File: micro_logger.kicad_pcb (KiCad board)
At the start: 2 copper layers, 16.8 x 27.4 mm, 25 parts, among them J3 ISP, J4 Conn_01x02, J5 DM3AT-SF-PEJM5, SW2 SW_Push, U1 MIC5205-3.3, U2 MPU-9250, U3 ATMEGA328-AU, Y1 Crystal_GND2

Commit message: updated shift logic
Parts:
- removed G***: LOGO, Symbol:gait_logo
- added C11: .1uF, Capacitor_SMD:C_0603_1608Metric, F.Cu at (150.7, 101.8)
- added C12: .1uF, Capacitor_SMD:C_0603_1608Metric, F.Cu at (148.3, 101.0)
- added C13: 100pF, Capacitor_SMD:C_0603_1608Metric, F.Cu at (140.8, 91.2)
- added C7: 1uF, Capacitor_SMD:C_0603_1608Metric, F.Cu at (141.3, 100.4)
- added R5: 10K, Resistor_SMD:R_0805_2012Metric, F.Cu at (140.9, 97.0)
- added R6: 10K, Resistor_SMD:R_0805_2012Metric, F.Cu at (146.5, 94.7)
- added R7: 200K, Resistor_SMD:R_0805_2012Metric, F.Cu at (149.2, 97.3)
- added U4: ICM-20948, components:ICM-20948, F.Cu at (145.2, 100.1)
- added U5: PCA9306, Package_SO:VSSOP-8_2.3x2mm_P0.5mm, F.Cu at (144.3, 94.6)
- C2: value 10nF -> 1uF
- R1, R2: value 10k -> 10K
- R4: footprint Resistor_SMD:R_0805_2012Metric_Pad1.15x1.40mm_HandSolder -> Resistor_SMD:R_0805_2012Metric
- U2: value MPU-9250 -> TLV70218_SOT23-5; footprint Package_DFN_QFN:QFN-24-1EP_3x3mm_P0.4mm_EP1.75x1.6mm -> Package_TO_SOT_SMD:SOT-23-5
- moved R9 16.6 mm to (148.5, 80.0), turned to 270 degrees
- moved C8 14.0 mm to (140.7, 82.4), turned to 180 degrees
- moved C2 10.0 mm to (141.4, 98.9), turned to 180 degrees
- moved C5 8.14 mm to (141.3, 102.0), turned to 0 degrees
- moved C6 7.23 mm to (150.7, 100.2)
- moved R2 5.80 mm to (149.3, 95.2), turned to 180 degrees
- moved U2 5.64 mm to (140.9, 94.1), turned to 180 degrees
- moved C9 3.57 mm to (139.7, 85.6)
- moved C1 2.38 mm to (144.5, 79.4)
- moved SW2 1.75 mm to (153.7, 99.1), turned to 270 degrees
- moved R1 1.74 mm to (149.3, 93.3)
- moved C3 1.46 mm to (140.0, 77.9)
- moved U1 1.20 mm to (147.4, 75.7)
- moved R4 0.77 mm to (153.1, 94.8)
- moved J3 0.67 mm to (150.9, 76.7)
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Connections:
- C2 pad 1: GND -> +3V3
- C2 pad 2: +3V3 -> GND
- C6 pad 1: GND -> +3V3
- C6 pad 2: +3V3 -> GND
- U2 pad 2: (no net) -> GND
- U2 pad 3: (no net) -> +3V3
- U2 pad 5: (no net) -> +1V8
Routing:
- net +1V8: track 0.00 -> 38.0 mm, vias 0 -> 4
- net GND: track 42.3 -> 71.0 mm, vias 14 -> 12
- net Net-(C13-Pad1): track 0.00 -> 14.2 mm, vias 0 -> 2
- net +3V3: track 81.2 -> 89.4 mm, vias 3 -> 4
- net MISO: track 17.8 -> 24.7 mm
- net /Ardunio/RESET: track 25.0 -> 31.4 mm, vias 2 -> 1
- net SCK: track 27.8 -> 33.0 mm, vias 1 -> 2
- net Net-(R5-Pad2): track 0.00 -> 5.20 mm
- net Net-(R6-Pad2): track 0.00 -> 4.33 mm
- net SDA_MPU: track 4.20 -> 8.33 mm
- net /Ardunio/D2: track 9.24 -> 12.9 mm, vias 0 -> 2
- net MOSI: track 18.6 -> 16.2 mm, vias 1 -> 2
- net VCC: track 17.0 -> 19.3 mm, vias 1 -> 2
- net Net-(U3-Pad7): track 2.78 -> 3.57 mm
- net Net-(C9-Pad1): track 2.53 -> 3.23 mm
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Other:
- board size 16.8 x 27.4 mm -> 17.5 x 29.5 mm

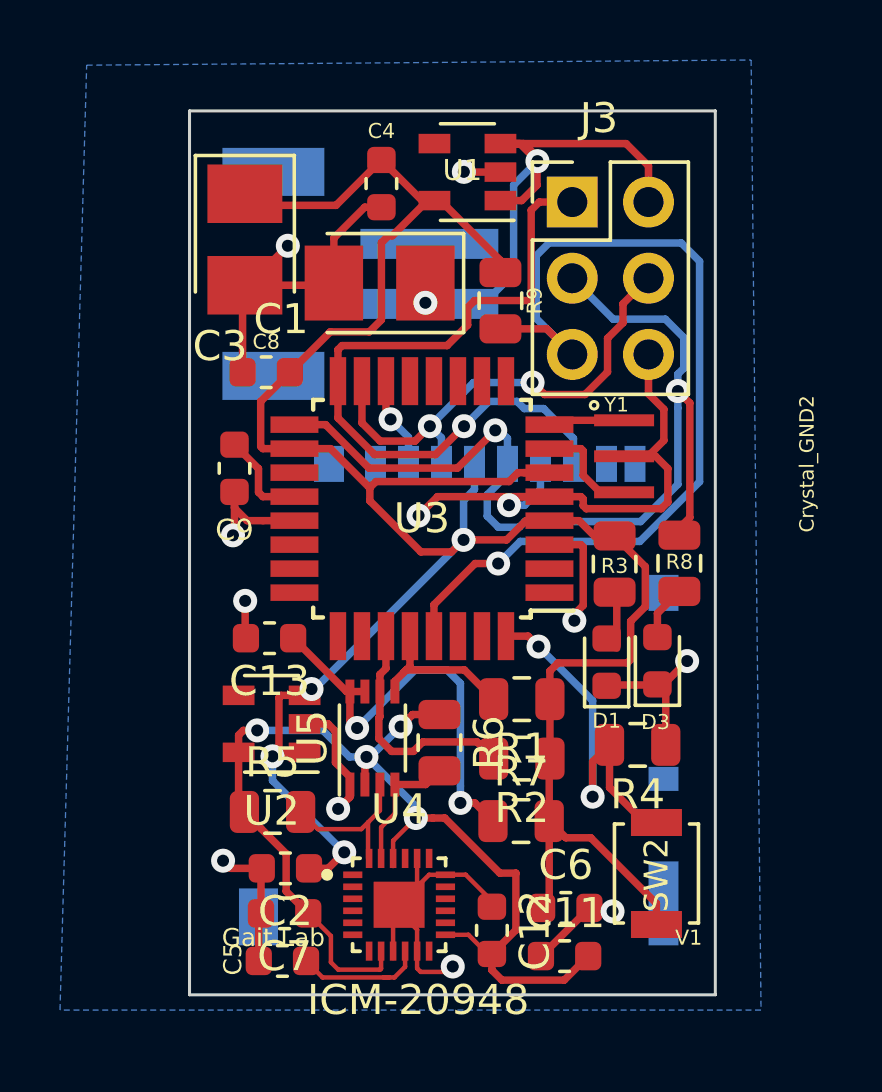
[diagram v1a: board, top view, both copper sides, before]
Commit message: updated layout
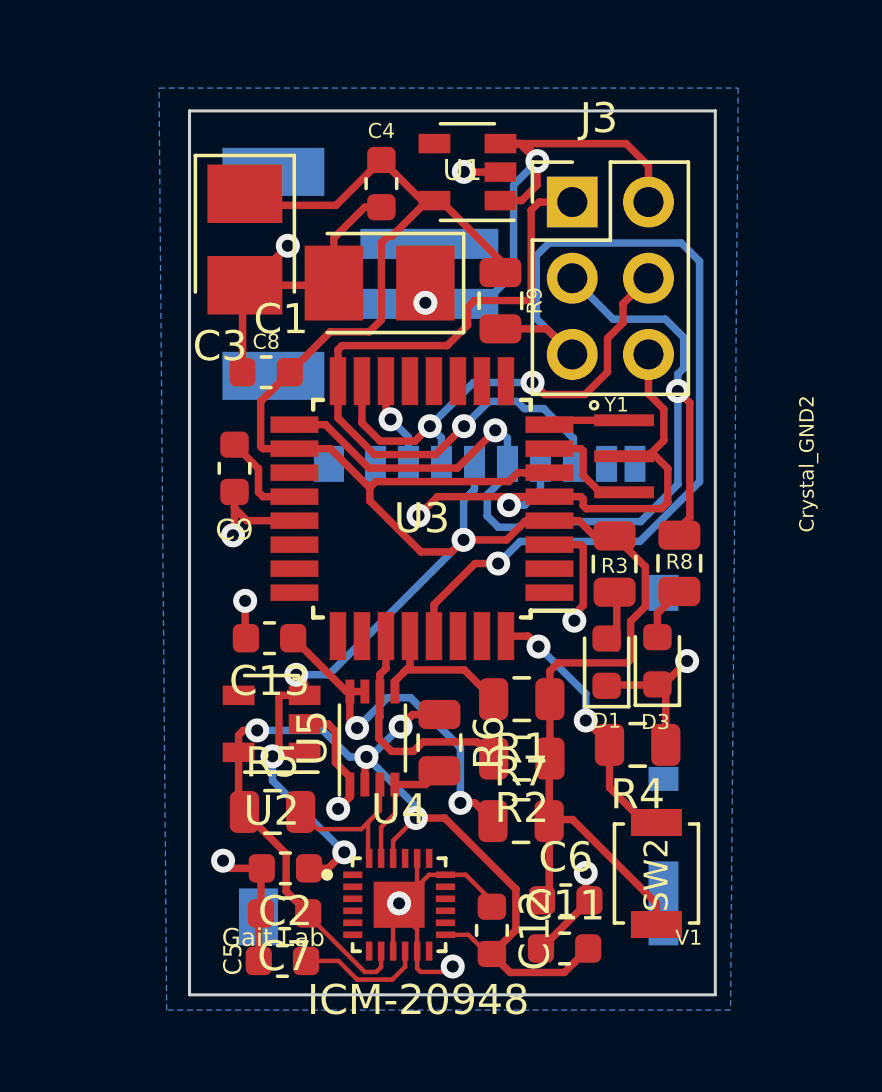
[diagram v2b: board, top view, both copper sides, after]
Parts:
- moved C11 0.25 mm to (150.7, 101.6)
- moved C6 0.25 mm to (150.7, 100.0)
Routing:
- net /Ardunio/D2: track 12.9 -> 9.48 mm
- net Net-(C13-Pad1): track 14.2 -> 12.2 mm
- net +1V8: track 38.0 -> 36.9 mm
- net +3V3: track 89.4 -> 90.3 mm
- net GND: track 71.0 -> 71.5 mm, vias 12 -> 13
